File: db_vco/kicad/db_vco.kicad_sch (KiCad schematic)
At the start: 38 parts, among them J1 V/OCT, J2 SOFT_SYNC, J3 TRIANGLE, J4 PWM, J5 HARD_SYNC, J6 SAWTOOTH, J7 SQUARE, J8 SINE, J9 LIN_FM, U1 AS3340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

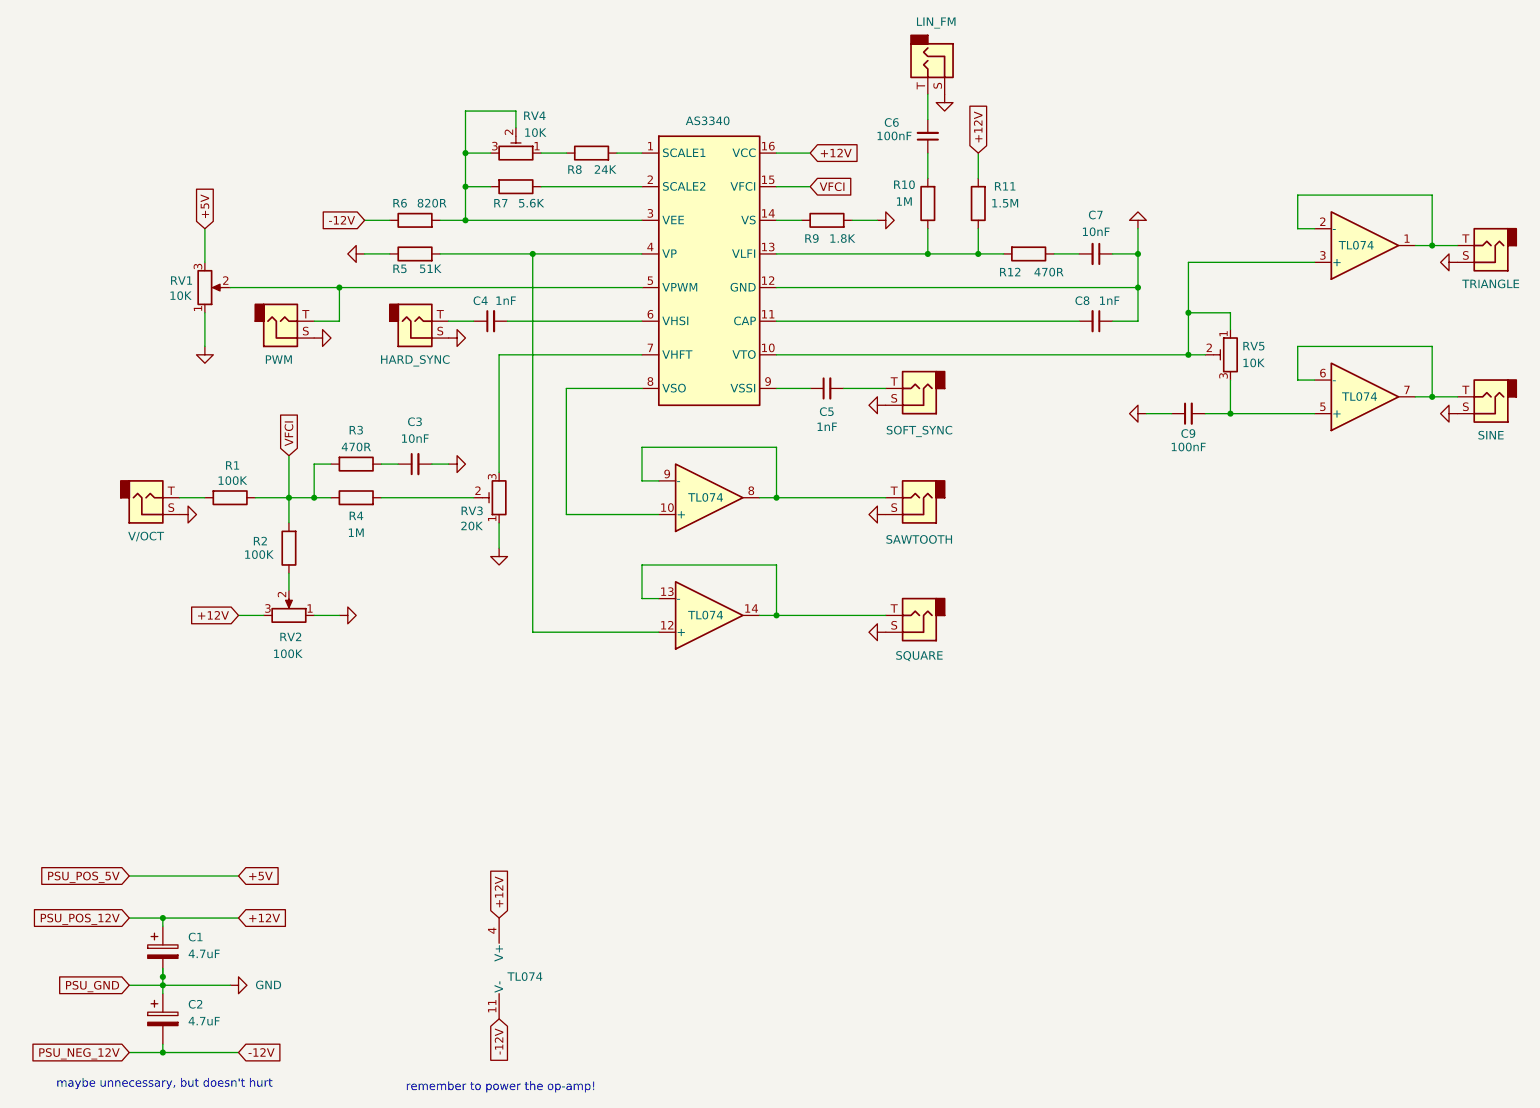
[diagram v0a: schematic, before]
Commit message: add vco more
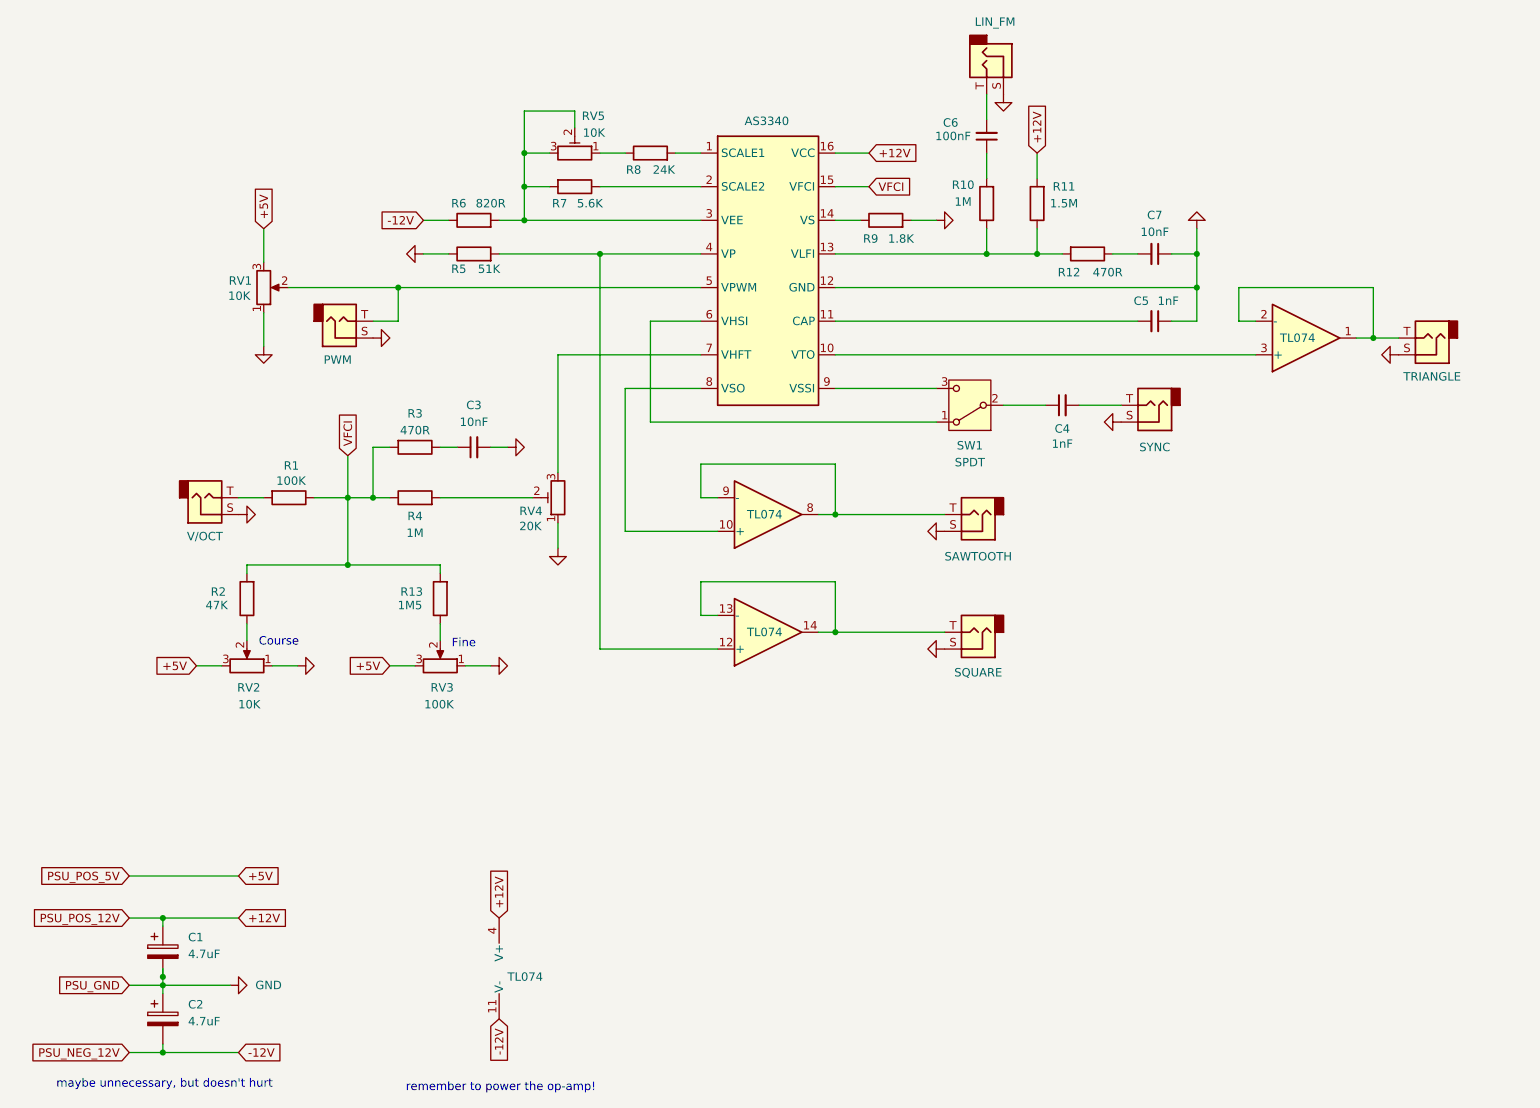
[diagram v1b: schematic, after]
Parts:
- removed C5: 1nF, symbol Device:C_Small
- removed C9: 100nF, symbol Device:C_Small
- removed J2: SOFT_SYNC, symbol Connector_Audio:AudioJack2
- removed J5: HARD_SYNC, symbol Connector_Audio:AudioJack2
- removed RV5: 10K, symbol Device:R_Potentiometer_Trim
- removed unit 2 of U2
- added R13: 1M5, symbol Device:R
- added RV3: 100K, symbol Device:R_Potentiometer
- added SW1: SPDT, symbol Switch:SW_SPDT
- J8: value SINE -> SYNC
- R2: value 100K -> 47K
- RV2: value 100K -> 10K
- renumbered C8 to C5, RV3 to RV4, RV4 to RV5
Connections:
- net +12V: no longer RV2.3
- net +5V: now also RV2.3, RV3.3
- net GND: now also RV3.1
- net VFCI: now also R13.2
- net at J8.T: now also C4.2
- net at U1.9 (VSSI): now also SW1.3 (C)
- net at C4.1: now also SW1.2 (B)
- net at U1.6 (VHSI): now also SW1.1 (A); no longer C4.2
- new net: R13.1, RV3.2
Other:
- note added: "Course"
- note added: "Fine"
- moved on the sheet: C3, C5, C6, C7, R1, R10, R11, R12, R3, R4, R5, R6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
